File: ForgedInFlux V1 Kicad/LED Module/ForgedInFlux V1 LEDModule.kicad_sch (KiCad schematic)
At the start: 30 parts

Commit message: Edited Schematic
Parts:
- removed D1, D10, D11, D12, D13, D14, D15, D2, D3, D4, D5, D6, D7, D8, D9: WS2812B, LED_SMD:LED_WS2812B_PLCC4_5.0x5.0mm_P3.2mm, symbol LED:WS2812B
- added D1, D10, D11, D12, D13, D14, D15, D2, D3, D4, D5, D6, D7, D8, D9: SK6812, LED_SMD:LED_SK6812_PLCC4_5.0x5.0mm_P3.2mm, symbol LED:SK6812
- C1: value C_Small -> 0.1uF
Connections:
- net GND: now also D1.1 (VSS), D10.1 (VSS), D11.1 (VSS), D12.1 (VSS), D13.1 (VSS), D14.1 (VSS), D15.1 (VSS), D2.1 (VSS), D3.1 (VSS), D4.1 (VSS), D5.1 (VSS), D6.1 (VSS), D7.1 (VSS), D8.1 (VSS), D9.1 (VSS)
- net LEDData: now also D1.2 (DIN)
- net at C9.2: now also D6.3 (VDD)
- net at C8.2: now also D13.3 (VDD)
- net at C14.2: now also D14.3 (VDD)
- net at C15.2: now also D15.3 (VDD)
- net at C11.2: now also D8.3 (VDD)
- net at C4.2: now also D4.3 (VDD)
- net at C2.2: now also D2.3 (VDD)
- net at C12.2: now also D9.3 (VDD)
- net at C1.2: now also D1.3 (VDD)
- net at C6.2: now also D11.3 (VDD)
- net at C13.2: now also D10.3 (VDD)
- net at C5.2: now also D5.3 (VDD)
- net at C10.2: now also D7.3 (VDD)
- net at C3.2: now also D3.3 (VDD)
- net at C7.2: now also D12.3 (VDD)
- new net: D10.4 (DOUT), D11.2 (DIN)
- new net: D11.4 (DOUT), D12.2 (DIN)
- new net: D12.4 (DOUT), D13.2 (DIN)
- new net: D5.4 (DOUT), D6.2 (DIN)
- new net: D6.4 (DOUT), D7.2 (DIN)
- new net: D14.4 (DOUT), D15.2 (DIN)
- new net: D7.4 (DOUT), D8.2 (DIN)
- new net: D2.4 (DOUT), D3.2 (DIN)
- new net: D3.4 (DOUT), D4.2 (DIN)
- new net: D13.4 (DOUT), D14.2 (DIN)
- new net: D1.4 (DOUT), D2.2 (DIN)
- new net: D8.4 (DOUT), D9.2 (DIN)
- new net: D10.2 (DIN), D9.4 (DOUT)
- new net: D4.4 (DOUT), D5.2 (DIN)

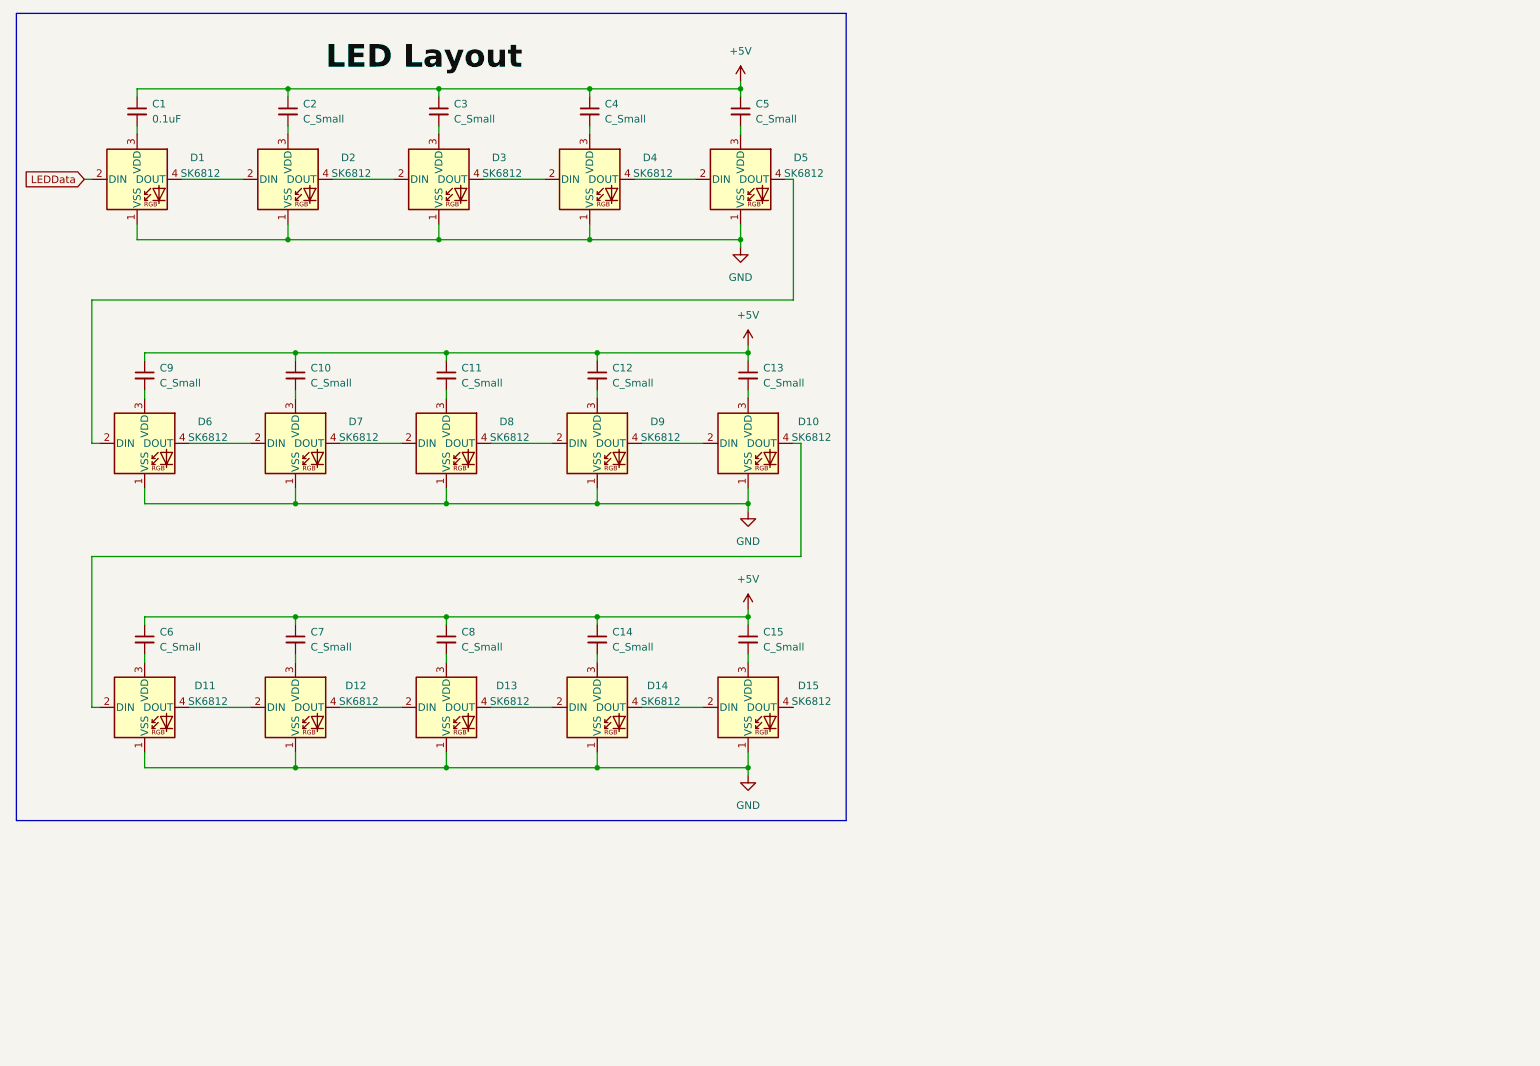
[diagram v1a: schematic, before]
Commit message: Started Creating LEDModulePCB
- Edge cuts recompleted with adjusted dimensions
- Created custom footprints and schematic symbol for LED Pads
- Completed Schematic
- Layed out parts components onto a pcb and done rough wire tracing.
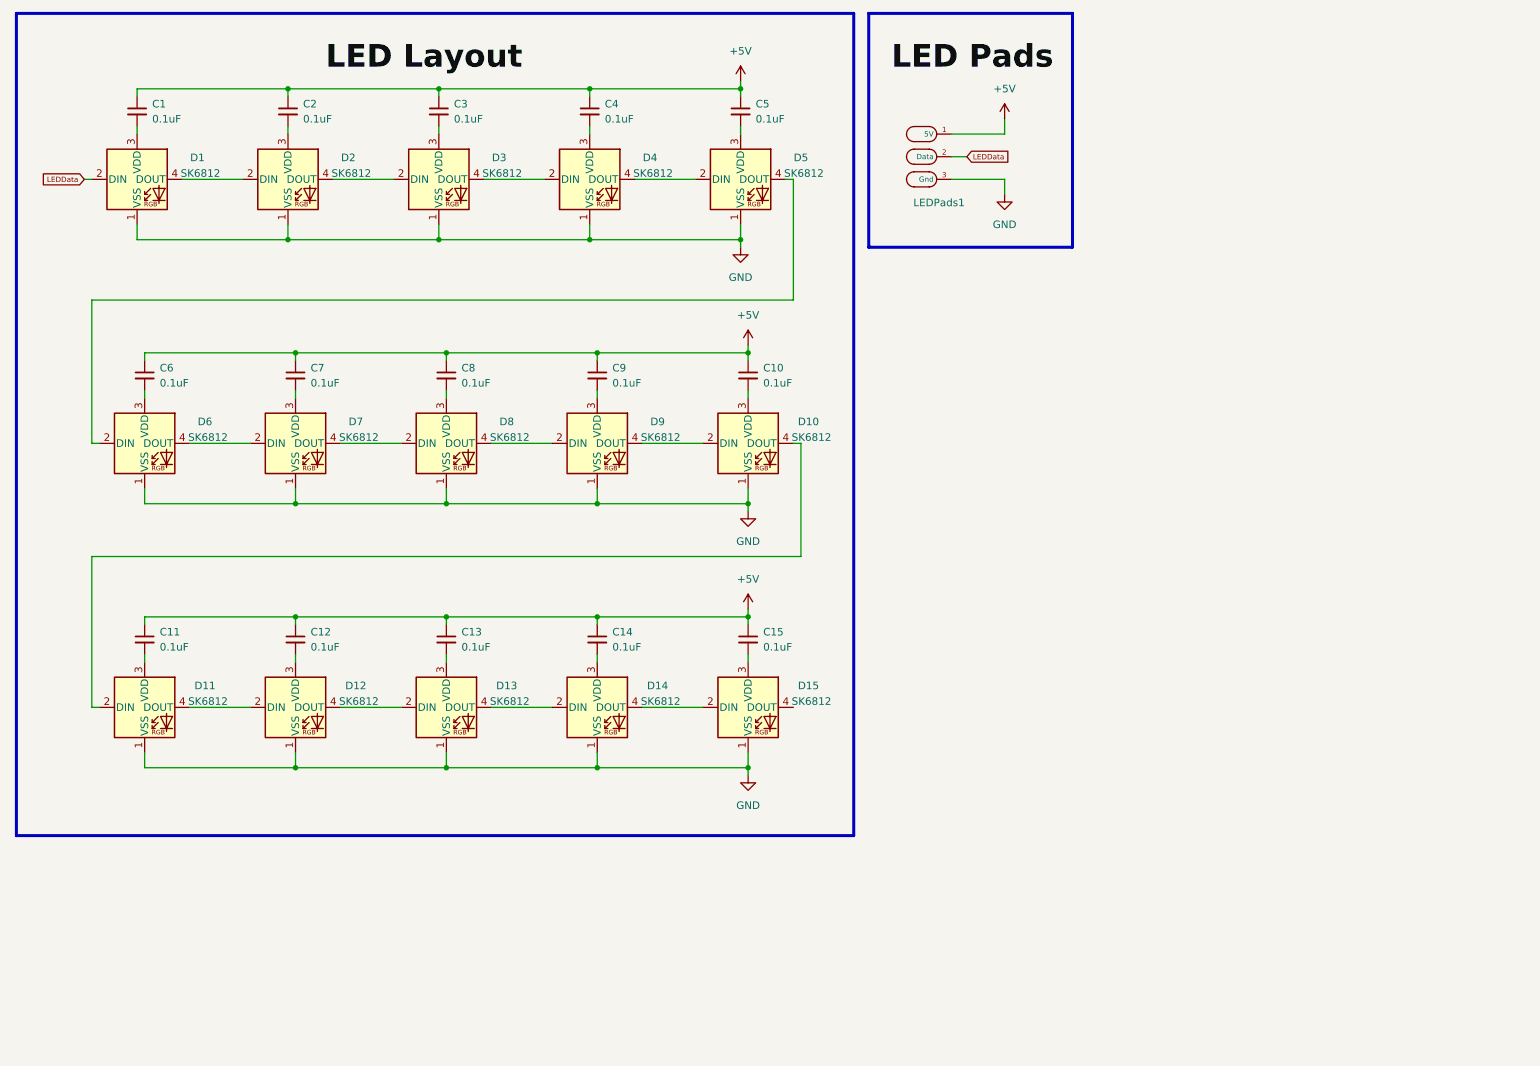
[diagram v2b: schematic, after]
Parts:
- added LEDPads1: ~, LEDModuleLibrary:Led Pads, symbol LEDModuleLibrary:LED_Pads
- C1: footprint (none) -> Capacitor_SMD:C_0603_1608Metric
- C10: renamed from C13; value C_Small -> 0.1uF; footprint (none) -> Capacitor_SMD:C_0603_1608Metric
- C11: renamed from C6; value C_Small -> 0.1uF; footprint (none) -> Capacitor_SMD:C_0603_1608Metric
- C12: renamed from C7; value C_Small -> 0.1uF; footprint (none) -> Capacitor_SMD:C_0603_1608Metric
- C13: renamed from C8; value C_Small -> 0.1uF; footprint (none) -> Capacitor_SMD:C_0603_1608Metric
- C14, C15, C2, C3, C4, C5: value C_Small -> 0.1uF; footprint (none) -> Capacitor_SMD:C_0603_1608Metric
- C6: renamed from C9; value C_Small -> 0.1uF; footprint (none) -> Capacitor_SMD:C_0603_1608Metric
- C7: renamed from C10; value C_Small -> 0.1uF; footprint (none) -> Capacitor_SMD:C_0603_1608Metric
- C8: renamed from C11; value C_Small -> 0.1uF; footprint (none) -> Capacitor_SMD:C_0603_1608Metric
- C9: renamed from C12; value C_Small -> 0.1uF; footprint (none) -> Capacitor_SMD:C_0603_1608Metric
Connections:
- net +5V: now also LEDPads1.1 (5V)
- net GND: now also LEDPads1.3 (Gnd)
- net LEDData: now also LEDPads1.2 (Data)

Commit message: Updates to schematic
- Changed Capacitor from Series to Parrallel
- Thickened PCB Traces
- Changed GND fill layers to 1 GND and 1 5V
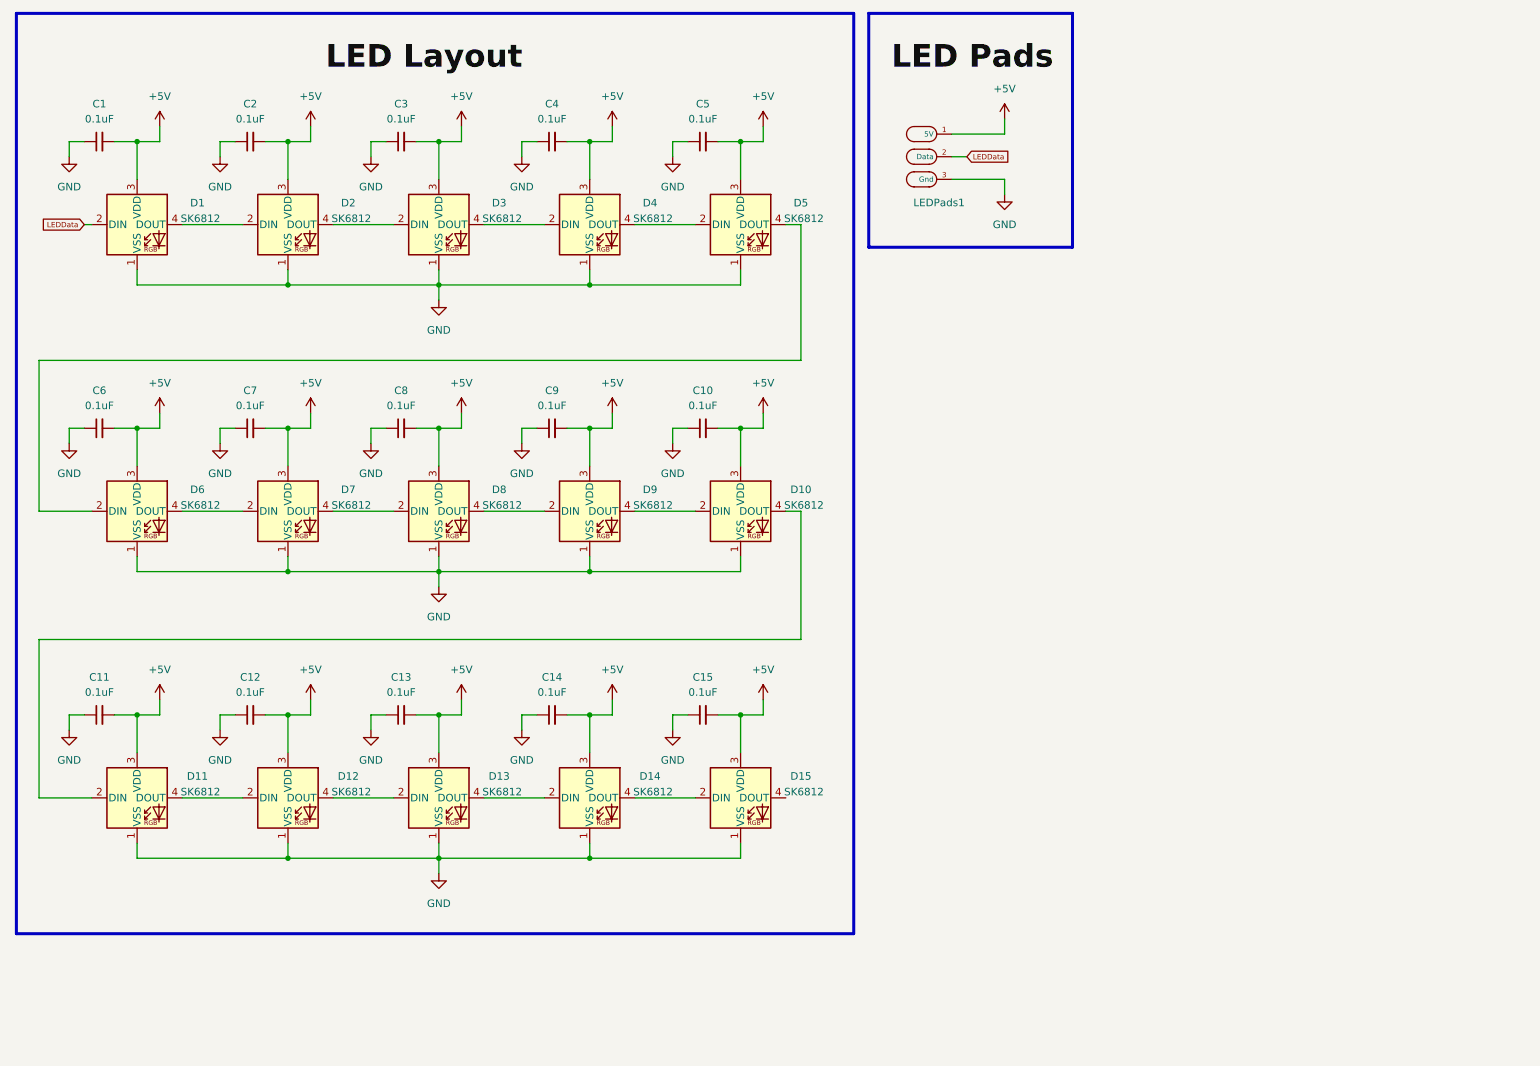
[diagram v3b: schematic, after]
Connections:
- net +5V: now also C1.2, C10.2, C11.2, C12.2, C13.2, C14.2, C15.2, C2.2, C3.2, C4.2, C5.2, C6.2, C7.2, C8.2, C9.2, D1.3 (VDD), D10.3 (VDD), D11.3 (VDD), D12.3 (VDD), D13.3 (VDD), D14.3 (VDD), D15.3 (VDD), D2.3 (VDD), D3.3 (VDD), D4.3 (VDD), D5.3 (VDD), D6.3 (VDD), D7.3 (VDD), D8.3 (VDD), D9.3 (VDD); no longer C1.1, C10.1, C11.1, C12.1, C13.1, C14.1, C15.1, C2.1, C3.1, C4.1, C5.1, C6.1, C7.1, C8.1, C9.1
- net GND: now also C1.1, C10.1, C11.1, C12.1, C13.1, C14.1, C15.1, C2.1, C3.1, C4.1, C5.1, C6.1, C7.1, C8.1, C9.1
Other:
- moved on the sheet: C1, D1, D2, D3, D4, D5

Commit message: Redesigned PCB
- Components changed for hand solderable parts
- Resistor in future will need to be exchanged for one that can handle more wattage.
- In future more clearance will be needed for top right LED.
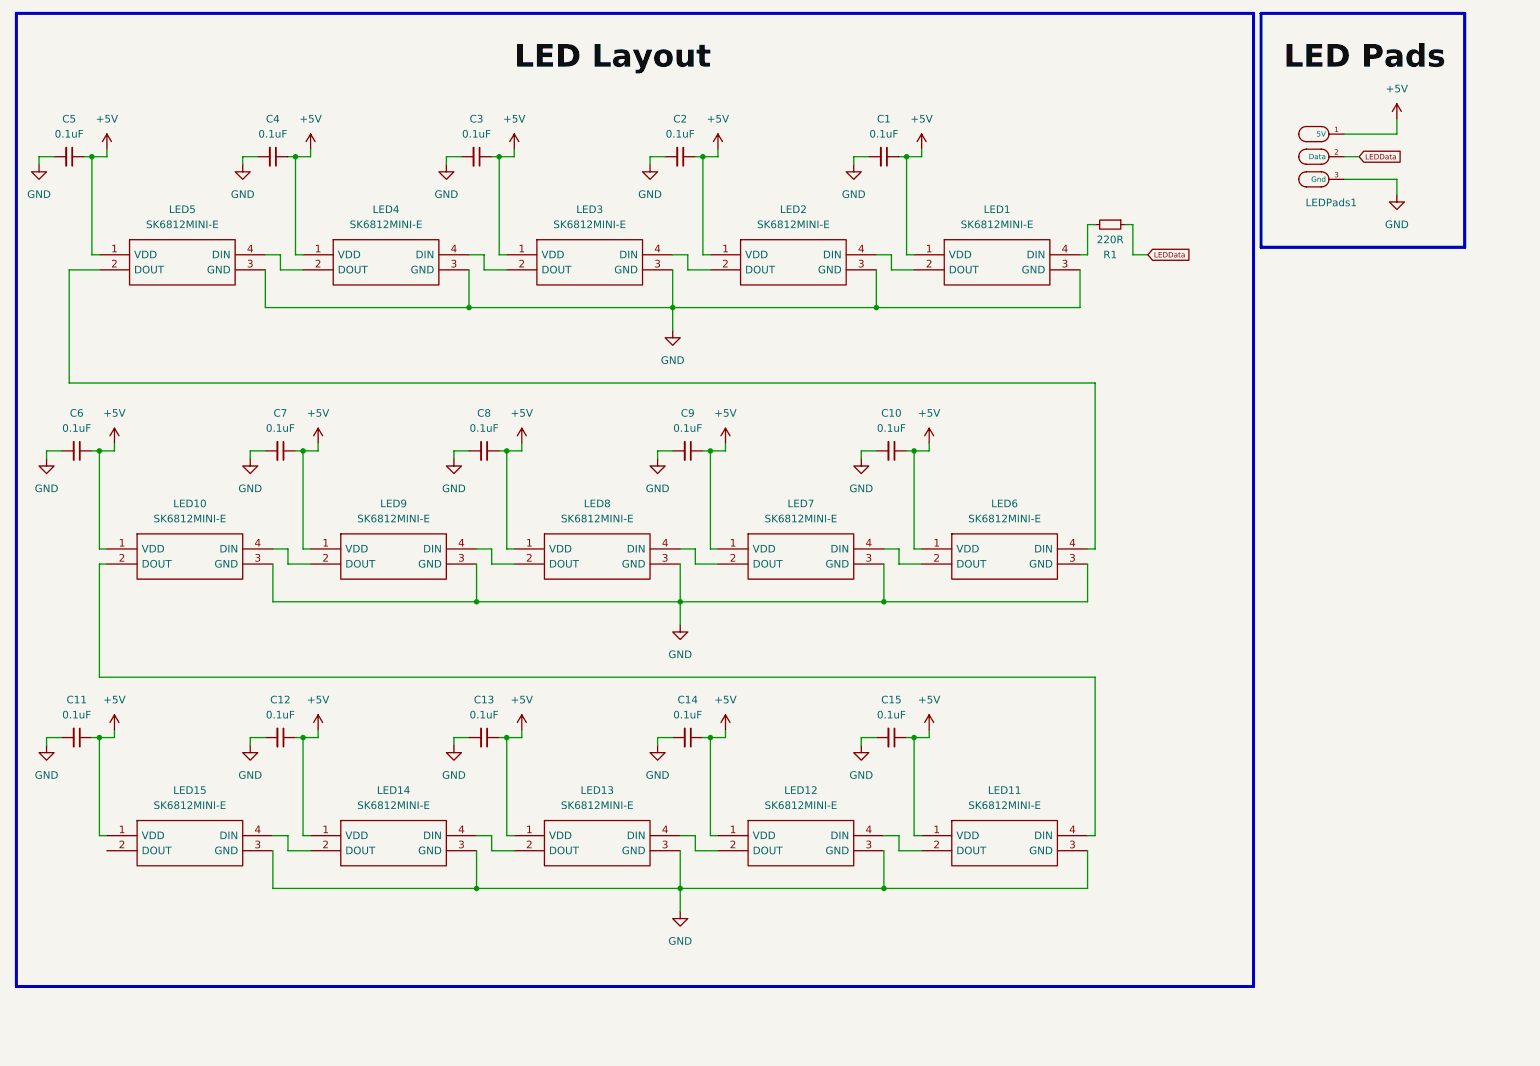
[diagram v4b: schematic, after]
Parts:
- removed D1, D10, D11, D12, D13, D14, D15, D2, D3, D4, D5, D6, D7, D8, D9: SK6812, LED_SMD:LED_SK6812_PLCC4_5.0x5.0mm_P3.2mm, symbol LED:SK6812
- added LED1, LED10, LED11, LED12, LED13, LED14, LED15, LED2, LED3, LED4, LED5, LED6, LED7, LED8, LED9: SK6812MINI-E, LEDModuleLibrary:SK6812-MINI-E, symbol LEDModuleLibrary:SK6812MINI-E
- added R1: 220R, Resistor_SMD:R_0805_2012Metric_Pad1.20x1.40mm_HandSolder, symbol Device:R_Small
- C1, C10, C11, C12, C13, C14, C15, C2, C3, C4, C5, C6, C7, C8, C9: footprint Capacitor_SMD:C_0603_1608Metric -> Capacitor_SMD:C_0805_2012Metric_Pad1.18x1.45mm_HandSolder
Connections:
- net +5V: now also C1.1, C10.1, C11.1, C12.1, C13.1, C14.1, C15.1, C2.1, C3.1, C4.1, C5.1, C6.1, C7.1, C8.1, C9.1, LED1.1 (VDD), LED10.1 (VDD), LED11.1 (VDD), LED12.1 (VDD), LED13.1 (VDD), LED14.1 (VDD), LED15.1 (VDD), LED2.1 (VDD), LED3.1 (VDD), LED4.1 (VDD), LED5.1 (VDD), LED6.1 (VDD), LED7.1 (VDD), LED8.1 (VDD), LED9.1 (VDD); no longer C1.2, C10.2, C11.2, C12.2, C13.2, C14.2, C15.2, C2.2, C3.2, C4.2, C5.2, C6.2, C7.2, C8.2, C9.2
- net GND: now also C1.2, C10.2, C11.2, C12.2, C13.2, C14.2, C15.2, C2.2, C3.2, C4.2, C5.2, C6.2, C7.2, C8.2, C9.2, LED1.3 (GND), LED10.3 (GND), LED11.3 (GND), LED12.3 (GND), LED13.3 (GND), LED14.3 (GND), LED15.3 (GND), LED2.3 (GND), LED3.3 (GND), LED4.3 (GND), LED5.3 (GND), LED6.3 (GND), LED7.3 (GND), LED8.3 (GND), LED9.3 (GND); no longer C1.1, C10.1, C11.1, C12.1, C13.1, C14.1, C15.1, C2.1, C3.1, C4.1, C5.1, C6.1, C7.1, C8.1, C9.1
- net LEDData: now also R1.1
- new net: LED8.2 (DOUT), LED9.4 (DIN)
- new net: LED7.2 (DOUT), LED8.4 (DIN)
- new net: LED3.2 (DOUT), LED4.4 (DIN)
- new net: LED2.2 (DOUT), LED3.4 (DIN)
- new net: LED1.2 (DOUT), LED2.4 (DIN)
- new net: LED1.4 (DIN), R1.2
- new net: LED4.2 (DOUT), LED5.4 (DIN)
- new net: LED13.2 (DOUT), LED14.4 (DIN)
- new net: LED12.2 (DOUT), LED13.4 (DIN)
- new net: LED6.2 (DOUT), LED7.4 (DIN)
- new net: LED5.2 (DOUT), LED6.4 (DIN)
- new net: LED10.4 (DIN), LED9.2 (DOUT)
- new net: LED11.2 (DOUT), LED12.4 (DIN)
- new net: LED14.2 (DOUT), LED15.4 (DIN)
- new net: LED10.2 (DOUT), LED11.4 (DIN)
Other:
- moved on the sheet: LEDPads1

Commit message: Updated design
- Full 1w SMD Resistor
- Satsified tolerances on LEDS and board edgecuts.
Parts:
- R1: footprint Resistor_SMD:R_0805_2012Metric_Pad1.20x1.40mm_HandSolder -> Resistor_SMD:R_2512_6332Metric_Pad1.40x3.35mm_HandSolder
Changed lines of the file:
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@@
 			)
 		)
-		(property "Footprint" "Resistor_SMD:R_0805_2012Metric_Pad1.20x1.40mm_HandSolder"
+		(property "Footprint" "Resistor_SMD:R_2512_6332Metric_Pad1.40x3.35mm_HandSolder"
 			(at 198.12 49.53 0)
 			(effects

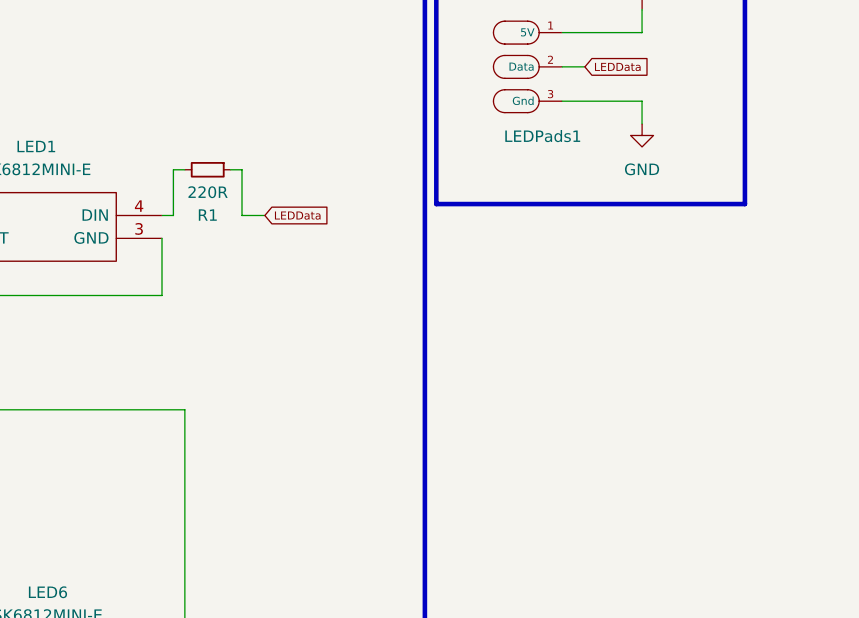
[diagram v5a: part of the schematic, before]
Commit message: Changes
- removed 1w resistor (not required for sk6812 mini-e leds)
added mounting holes that align with control unit internal standoffs
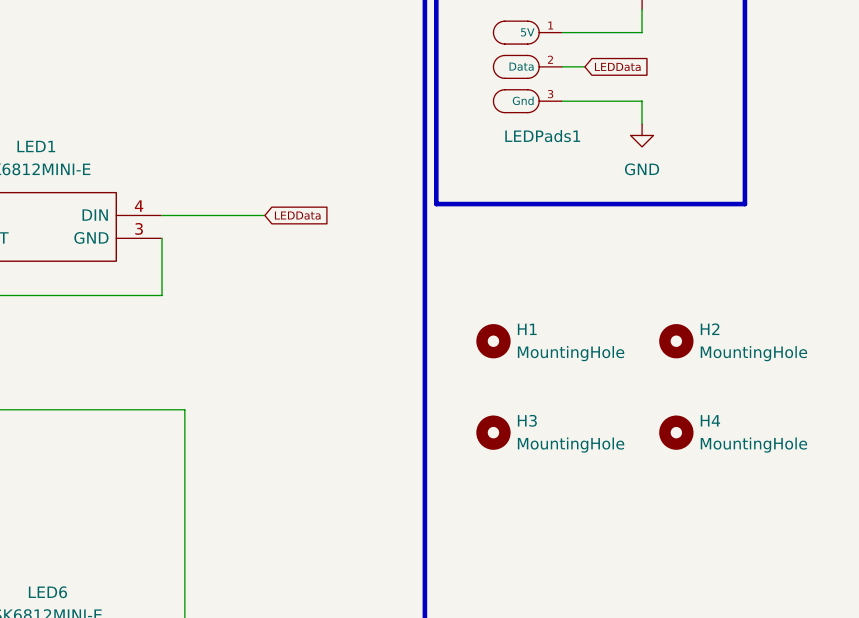
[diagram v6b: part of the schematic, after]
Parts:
- removed R1: 220R, Resistor_SMD:R_2512_6332Metric_Pad1.40x3.35mm_HandSolder, symbol Device:R_Small
- added H1, H2, H3, H4: MountingHole, MountingHole:MountingHole_3.2mm_M3_Pad, symbol Mechanical:MountingHole
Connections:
- net LEDData: now also LED1.4 (DIN)
